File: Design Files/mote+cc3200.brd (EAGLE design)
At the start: 100 x 80 mm, 13 parts, among them IC1 TPS6306X, U1 CC3200

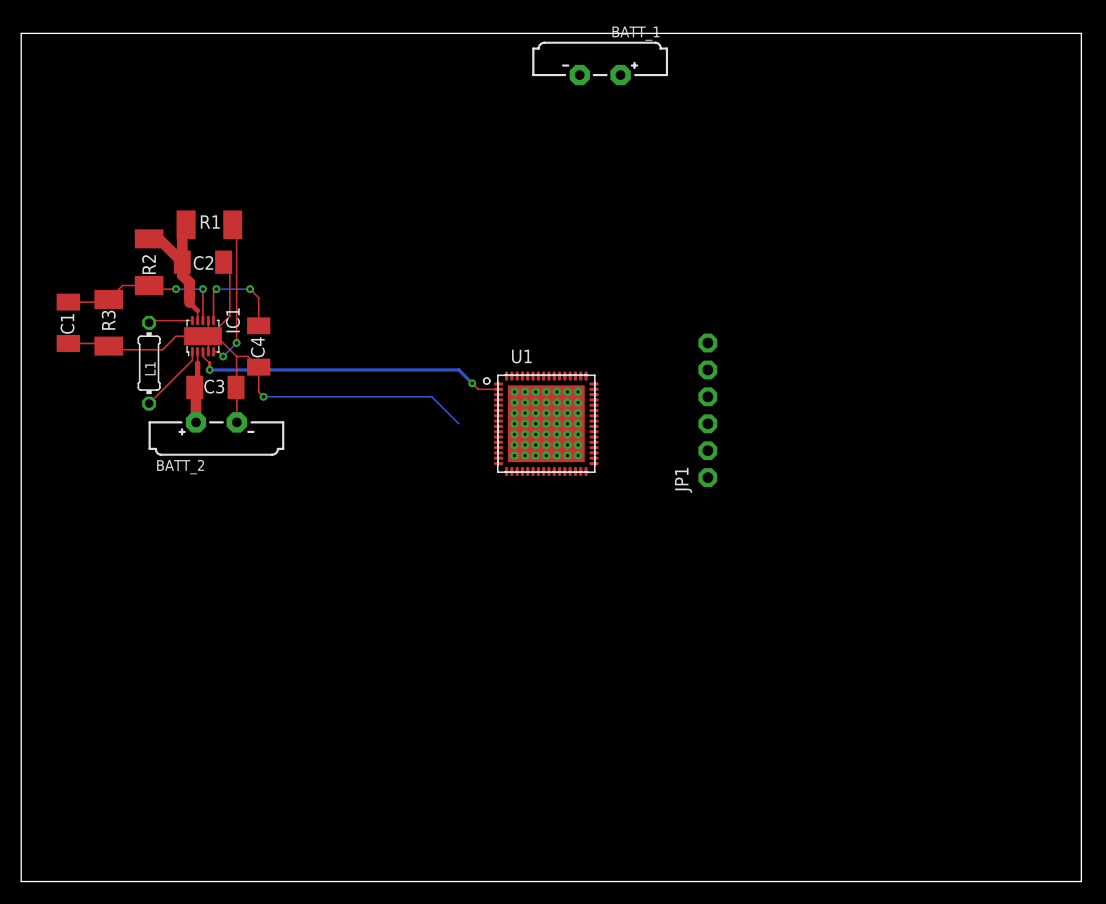
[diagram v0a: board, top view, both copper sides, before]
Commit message: Updated Design Files and Libraries
Some libraries included in the design were added.
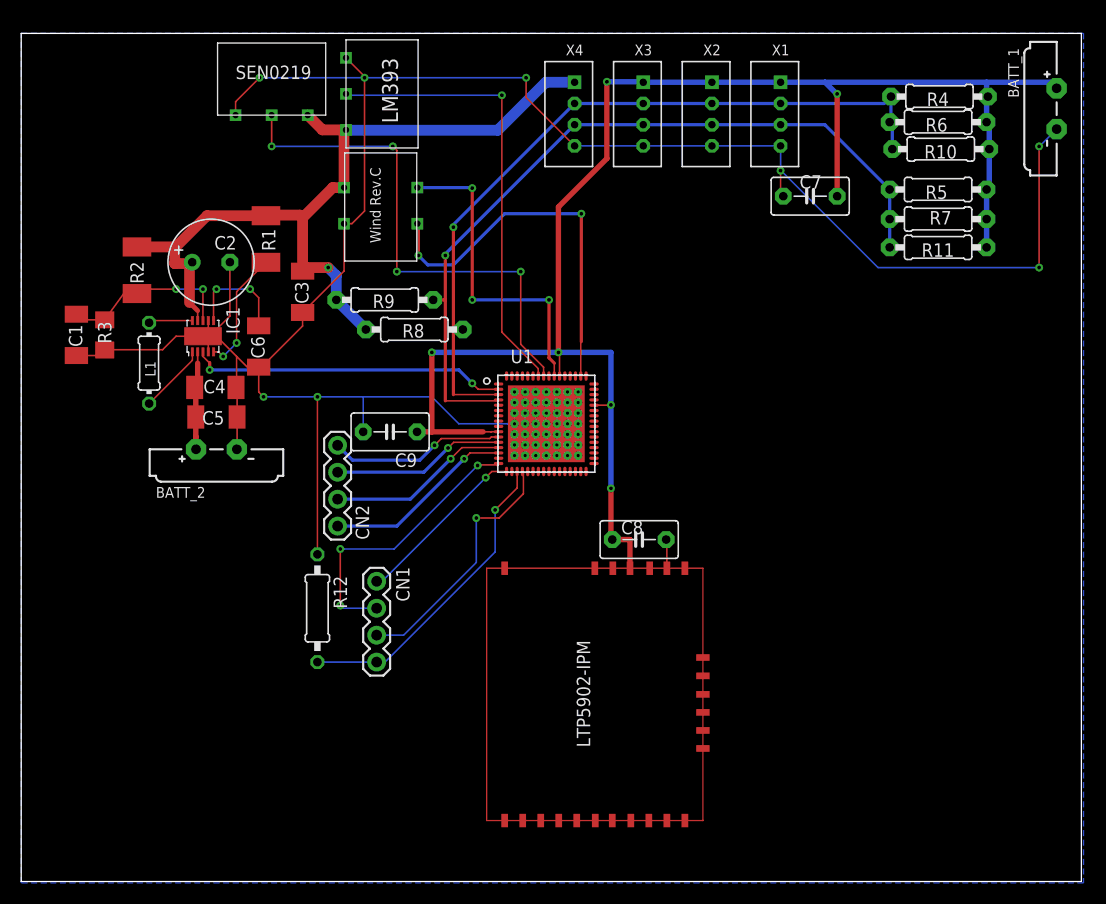
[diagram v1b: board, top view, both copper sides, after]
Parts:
- removed JP1: (no value), adafruit:1X06-CLEANBIG
- added C5: 10 uF, eagle-ltspice:C1808
- added C6: 0.1 uF, rcl:C1808
- added C7: 0.22 uF, capacitor-wima:C5B3.5
- added C8, C9: 0.1uF, capacitor-wima:C5B3.5
- added CN1: JTAG, adafruit:1X04-BIG
- added CN2: FLASH, adafruit:1X04-BIG
- added R10, R11, R4, R5, R6, R7, R8, R9: 2.2K, adafruit:0207/9
- added R12: 100K, resistor:0207/10
- added U2: WIND, WINDc:WIND
- added U3: SEN0219, SEN0219c:SEN0219
- added U4: LM393, LM393c:LM393
- added U5: LTP5902, LTP5902c:LTP5901
- added X1: HIH8121-021-001, con-JST PH:B4B-PH-K-S
- added X2: OPT3001, con-JST PH:B4B-PH-K-S
- added X3: ADXL362, con-JST PH:B4B-PH-K-S
- added X4: SEN0322, con-JST PH:B4B-PH-K-S
- C2: value 66 uF -> 56 uF; device eagle-ltspice:C1808 -> rcl:E3,5-8
- C3: value 20 uF -> 10 uF
- C4: value 0.1 uF -> 10 uF
- R1, R2: device eagle-ltspice:R2010 -> rcl:R5025
- R3: device eagle-ltspice:R2010 -> rcl:R1206
- moved BATT_1 41.9 mm to (96.3, 72.9), turned to 270 degrees
- moved C3 12.2 mm to (26.5, 55.6), turned to 270 degrees
- moved C4 5.62 mm to (18.3, 46.6), turned to 0 degrees
- moved R1 5.50 mm to (23.1, 60.6), turned to 90 degrees
- moved BATT_2 2.54 mm to (18.4, 39.4)
- moved C1 1.37 mm to (5.21, 51.6)
- moved R2 1.37 mm to (10.9, 57.7)
- moved R3 1.20 mm to (7.87, 51.6)
- moved C2 0.76 mm to (17.9, 58.4)
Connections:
- new net 3.3V: U5.P$1, U5.P$10, U5.P$11, U5.P$9
- new net AO_0S: U1.50, U2.P$4
- new net AO_1S: U1.55, U2.P$3
- new net AO_2S: U1.57, U3.P$2
- new net AO_3S: U1.58, U4.P$2
- new net DO_0: U5.P$2
- new net DO_1: U5.P$3
- new net FLASH_P_ENN: U5.P$21
- new net FLS_SPI_CLK: CN2.1, U1.11
- new net FLS_SPI_CS: CN2.4, U1.14
- new net FLS_SPI_DIN: CN2.3, U1.13
- new net FLS_SPI_DOUT: CN2.2, U1.12
- new net IPCS_MISO: U5.P$14
- new net IPCS_MOSI: U5.P$16
- new net IPCS_SCK: U5.P$17
- new net IPCS_SSN: U5.P$19
- new net N$1: CN1.4, R12.2, U1.19
- new net N$2: CN1.3, U1.20
- new net N$3: CN1.2, U1.16
- new net N$4: CN1.1, U1.17
- net +3.3V: now also C7.1, C8.2, C9.1, R10.1, R11.1, R4.1, R5.1, R6.1, R7.1, U5.P$22, X1.1, X2.1, X3.1
- net +3.6V: now also C4.1, C5.1; no longer C3.1
- net +5V: now also C2.+, C3.1, R8.1, R9.1, U2.P$1, U3.P$1, U4.P$1, X4.1; no longer C2.1
- net GND: now also C2.-, C5.2, C6.2, C7.2, C8.1, C9.2, R12.1, U2.P$2, U3.P$3, U4.P$3, U5.P$15, U5.P$18, U5.P$20, U5.P$23, U5.P$24, X1.4, X2.4, X3.4, X4.4; no longer C2.2
- net SCL: now also R10.2, R4.2, R6.2, R8.2, X1.2, X2.2, X3.2, X4.2
- net SDA: now also R11.2, R5.2, R7.2, R9.2, X1.3, X2.3, X3.3, X4.3
- net VAUX_TPS: now also C6.1; no longer C4.1
- net WK_UP: now also U5.P$4
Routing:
- net GND: track 60.9 -> 252.4 mm, vias 1 -> 8
- net +3.3V: track 0.00 -> 154.7 mm, vias 0 -> 6
- net SDA: track 0.00 -> 75.0 mm, vias 0 -> 1
- net SCL: track 0.00 -> 72.6 mm, vias 0 -> 1
- net +5V: track 13.8 -> 79.2 mm, vias 0 -> 1
- net AO_2S: track 0.00 -> 48.8 mm, vias 0 -> 4
- net AO_3S: track 0.00 -> 42.7 mm, vias 0 -> 1
- net AO_0S: track 0.00 -> 36.1 mm, vias 0 -> 2
- net AO_1S: track 0.00 -> 30.4 mm, vias 0 -> 3
- net N$1: track 0.00 -> 29.5 mm, vias 0 -> 1
- net N$3: track 0.00 -> 27.2 mm, vias 0 -> 3
- net N$2: track 0.00 -> 24.0 mm, vias 0 -> 1
- net FLS_SPI_CS: track 0.00 -> 18.0 mm, vias 0 -> 1
- net FLS_SPI_DIN: track 0.00 -> 17.2 mm, vias 0 -> 1
- net FLS_SPI_CLK: track 0.00 -> 16.7 mm, vias 0 -> 1
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- added copper zone on layer 16, net GND

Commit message: Updated design files.
Overwritten original mote+cc3200 files to revision 1.5. Added CAM data files in zip folder for PCB fabrication.
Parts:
- removed CN2: FLASH, adafruit:1X04-BIG
- removed R11: 2.2K, adafruit:0207/9
- removed R12: 100K, resistor:0207/10
- removed R2: 1 M, rcl:R5025
- removed U1: CC3200, CC3200:RGC0064A
- removed X4: SEN0322, con-JST PH:B4B-PH-K-S
- added AC1: ADXL345, ADXL345:CC-14-1
- added C10, C11: 10 pF, eagle-ltspice:C1808
- added C12, C16, C17, C19, C20, C22: 0.1 uF, rcl:C1808
- added C13: 0.1uF, capacitor-wima:C5B3.5
- added C14: 2.2 uF, eagle-ltspice:C1808
- added C15: 0.22 uF, capacitor-wima:C5B3.5
- added C18, C21: 10 uF, eagle-ltspice:C1808
- added D1: SP1002-01JTG, SamacSys_Parts:SOT132P220X110-3N
- added HDR1: 87831-1020, SamacSys_Parts:SHDR10W55P200_2X5_1265X630X640
- added IC2: W25Q80DLSNIG_TR, SamacSys_Parts:SOIC127P600X175-8N
- added JP1, JP2, JP3: (no value), eagle-ltspice:R0201
- added L2, L3: 2.2 uH, rcl:L3216C
- added LED1: 156120RS75000, SamacSys_Parts:LEDM3216X130N
- added PB1: FSMSM, SamacSys_Parts:FSMSM
- added Q1, Q2, Q3, Q4: FQU20N06LTU, SamacSys_Parts:TO229P250X658X985-3P
- added Q5: DMN2004WK-7, SamacSys_Parts:SC70-3_DCK
- added S1: EG1224, SamacSys_Parts:EG1224
- added U6: LM393, LM393c:LM393
- added Y1: 32.768 KHz, crystal-geyer_V1_0:7.0X5.0
- BATT_2: value BATTERY_BR1225/FA -> 12BH23P-GR; device 52101-101-REV-A_v16:BATTERY_BR1225/FA -> SamacSys_Parts:12BH23PGR
- C1: value 10 pF -> 10 uF
- C2: value 56 uF -> 10 uF; device rcl:E3,5-8 -> eagle-ltspice:C1808
- C3: value 10 uF -> 0.1uF; device eagle-ltspice:C1808 -> capacitor-wima:C5B3.5
- C4, C5: value 10 uF -> 0.1 uF; device eagle-ltspice:C1808 -> rcl:C1808
- C7: value 0.22 uF -> 10 pF; device capacitor-wima:C5B3.5 -> eagle-ltspice:C1808
- C8: value 0.1uF -> 56 uF; device capacitor-wima:C5B3.5 -> rcl:E3,5-8
- C9: value 0.1uF -> 10 uF; device capacitor-wima:C5B3.5 -> eagle-ltspice:C1808
- R1: value 1 M -> 100K; device rcl:R5025 -> resistor:0207/10
- R10: value 2.2K -> 270; device adafruit:0207/9 -> Resistor_Capacitor:RES_1206
- R3: value 111 K -> 1 M; device rcl:R1206 -> rcl:R5025
- R4: value 2.2K -> 111 K; device adafruit:0207/9 -> rcl:R1206
- R5: value 2.2K -> 1 M; device adafruit:0207/9 -> rcl:R5025
- R6, R7, R8: value 2.2K -> 100 K; device adafruit:0207/9 -> rcl:R1206
- R9: value 2.2K -> 10 K; device adafruit:0207/9 -> Resistor_Capacitor:RES_1206
- U2: value WIND -> Value; device WINDc:WIND -> CC3200:RGC0064A
- U3: value SEN0219 -> LTP5902; device SEN0219c:SEN0219 -> LTP5902c:LTP5902-MMCX
- U4: value LM393 -> WIND; device LM393c:LM393 -> WINDc:WIND
- U5: value LTP5902 -> SEN0219; device LTP5902c:LTP5901 -> SEN0219c:SEN0219
- X3: value ADXL362 -> SEN0322
- moved R4 87.6 mm to (5.33, 41.4), turned to 90 degrees
- moved R5 82.4 mm to (6.22, 46.6), turned to 0 degrees
- moved U3 80.2 mm to (83.6, 22.4), turned to 0 degrees
- moved C7 75.6 mm to (2.54, 41.3), turned to 270 degrees
- moved R6 73.0 mm to (31.2, 23.9), turned to 0 degrees
- moved R7 70.5 mm to (26.8, 25.0), turned to 270 degrees
- moved U5 65.6 mm to (23.6, 75.7), turned to 270 degrees
- moved C8 46.0 mm to (13.8, 43.9), turned to 0 degrees
- moved C4 36.7 mm to (54.5, 53.0), turned to 90 degrees
- moved C5 35.8 mm to (48.1, 23.9)
- moved R9 35.7 mm to (54.7, 25.7)
- moved R1 31.5 mm to (23.6, 29.1), turned to 270 degrees
- moved BATT_2 29.1 mm to (29.4, 12.4), turned to 180 degrees
- moved C2 27.8 mm to (14.5, 30.9)
- moved U2 25.7 mm to (49.5, 43.2)
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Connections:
- removed net 3.3V: U5.P$1, U5.P$10, U5.P$11, U5.P$9
- removed net AO_0S: U1.50, U2.P$4
- removed net AO_1S: U1.55, U2.P$3
- removed net AO_2S: U1.57, U3.P$2
- removed net AO_3S: U1.58, U4.P$2
- removed net DCDC_ANA_SW: U1.38
- removed net DCDC_DIG_SW: U1.43
- removed net DO_0: U5.P$2
- removed net DO_1: U5.P$3
- removed net LDO_IN1: U1.36
- removed net LDO_IN2: U1.25
- removed net N$1: CN1.4, R12.2, U1.19
- removed net N$2: CN1.3, U1.20
- removed net N$3: CN1.2, U1.16
- removed net N$4: CN1.1, U1.17
- removed net VDD_DIG1: U1.9
- removed net VDD_DIG2: U1.56
- removed net VDD_PLL: U1.24
- removed net WK_UP: IC1.3, U1.2, U5.P$4
- new net DC_ANA2: JP2.1, U2.46
- new net DC_DIGSW: L3.2, U2.43
- new net GPIO12: Q4.1, U2.3
- new net GPIO13: Q1.1, U2.4
- new net GPIO14: Q2.1, U2.5
- new net GPIO15: Q3.1, U2.6
- new net GPIO2: U2.57, U4.P$4
- new net GPIO22: IC1.3, U2.15
- new net GPIO3: U2.58, U4.P$3
- new net GPIO31: JP2.2
- new net GPIO4: U2.59, U5.P$2
- new net GPIO5: U2.60, U6.P$2
- new net JTCK: JP1.2, U2.21
- new net L2_ANA: L2.2, U2.38
- new net LED1: LED1.2, R10.2
- new net Q1+: AC1.2, AC1.4, AC1.5, C15.2, Q1.2, U6.P$3, X1.4, X2.4
- new net Q2+: Q2.2, U4.P$2
- new net Q3+: Q3.2, U5.P$3
- new net Q4+: Q4.2, X3.4
- new net RESETN: HDR1.6, Q5.3, U3.P15
- new net RST_BTN: C13.2, PB1.1, Q5.1, R9.2
- new net TCK: CN1.4, JP1.1, R1.2, U2.19
- new net TDI: CN1.2, U2.16
- new net TDO: CN1.1, U2.17
- new net TMS: CN1.3, U2.20
- new net UARTC0_RX: HDR1.10, U2.8, U3.P32
- new net UARTC0_TX: HDR1.9, U2.7, U3.P31
- new net VCC_DCDC: JP3.2
- new net VDD_DIG: C16.1, C17.1, C18.1, L3.1, U2.56, U2.9
- new net VDD_PULL: C5.1, U2.24
- new net VIN_DCDC_PA: U2.39
- new net VSUPPLY: HDR1.7
- new net XTAL1: C11.1, U2.51, Y1.3
- new net XTAL2: C10.1, U2.52, Y1.1
- net +3.3V: now also AC1.1, C12.1, C14.1, C15.1, C3.1, D1.1, IC2.3, IC2.7, IC2.8, PB1.2, R8.2, S1.1, U2.10, U2.37, U2.44, U2.54, U3.P55, U6.P$1; no longer C7.1, C8.2, C9.1, R11.1, R4.1, R5.1, R6.1, R7.1, U1.10, U1.37, U1.39, U1.44, U1.54, U5.P$22, X3.1
- net +3.6V: now also BATT_2.2, C1.1, C2.1; no longer BATT_2.+, C4.1, C5.1
- net +5V: now also C8.+, C9.1, R3.2, R5.2, U5.P$1, X3.1; no longer C2.+, C3.1, R1.2, R2.2, R8.1, R9.1, U2.P$1, U3.P$1, X4.1
- net DCDC_PA_OUT: now also U2.42; no longer U1.42
- net DCDC_PA_SW_N: now also U2.41; no longer U1.41
- net DCDC_PA_SW_P: now also U2.40; no longer U1.40
- net FB_TPS: now also C7.1, R4.2, R5.1; no longer C1.1, R2.1, R3.2
- net FLASH_P_ENN: now also HDR1.2, U3.P51; no longer U5.P$21
- net FLS_SPI_CLK: now also IC2.6, R6.1, U2.11; no longer CN2.1, U1.11
- net FLS_SPI_CS: now also IC2.1, R8.1, U2.14; no longer CN2.4, U1.14
- net FLS_SPI_DIN: now also IC2.2, U2.13; no longer CN2.3, U1.13
- net FLS_SPI_DOUT: now also IC2.5, R7.1, U2.12; no longer CN2.2, U1.12
- net GND: now also BATT_2.1, C10.2, C11.2, C12.2, C13.1, C14.2, C16.2, C17.2, C18.2, C19.2, C2.2, C20.2, C21.2, C22.2, C8.-, D1.2, HDR1.8, IC2.4, LED1.1, Q1.3, Q2.3, Q3.3, Q4.3, Q5.2, R1.1, R4.1, R6.2, R7.2, R9.1, S1.2, U2.65, U2.V, U2.V_1, U2.V_10, U2.V_11, U2.V_12, U2.V_13, U2.V_14, U2.V_15, U2.V_16, U2.V_17, U2.V_18, U2.V_19, U2.V_2, U2.V_20, U2.V_21, U2.V_22, U2.V_23, U2.V_24, U2.V_25, U2.V_26, U2.V_27, U2.V_28, U2.V_29, U2.V_3, U2.V_30, U2.V_31, U2.V_32, U2.V_33, U2.V_34, U2.V_35, U2.V_36, U2.V_37, U2.V_38, U2.V_39, U2.V_4, U2.V_40, U2.V_41, U2.V_42, U2.V_43, U2.V_44, U2.V_45, U2.V_46, U2.V_47, U2.V_48, U2.V_5, U2.V_6, U2.V_7, U2.V_8, U2.V_9, U3.P1, U3.P11, U3.P20, U3.P30, U3.P34, U3.P37, U3.P42, U3.P49, U3.P56, U3.P66; no longer BATT_2.-, C2.-, C8.1, R12.1, R3.1, U1.65, U2.P$2, U3.P$3, U4.P$3, U5.P$15, U5.P$18, U5.P$20, U5.P$23, U5.P$24, X1.4, X2.4, X3.4, X4.4
- net IPCS_MISO: now also HDR1.5, U3.P33; no longer U5.P$14
- net IPCS_MOSI: now also U3.P35; no longer U5.P$16
- net IPCS_SCK: now also HDR1.3; no longer U5.P$17
- net IPCS_SSN: now also HDR1.1, U3.P39; no longer U5.P$19
- net PG_TPS: now also R3.1; no longer R1.1
- net SCL: now also AC1.14, U2.1; no longer R10.2, R4.2, R6.2, R8.2, U1.3, X4.2
- net SDA: now also AC1.13, U2.2; no longer R11.2, R5.2, R7.2, R9.2, U1.4, X4.3
- net VDD_ANA1: now also C19.1, C20.1, C21.1, C22.1, L2.1, U2.25, U2.36, U2.48; no longer U1.48
- net VDD_ANA2: now also JP3.1, U2.47; no longer U1.47
- net VDD_PA_IN: now also U2.33; no longer U1.33
- net VDD_RAM: now also C4.1, U2.49; no longer U1.49
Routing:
- net GND: track 252.4 -> 407.6 mm, vias 8 -> 14
- net +3.3V: track 154.7 -> 272.4 mm, vias 6 -> 10
- net UARTC0_RX: track 0.00 -> 110.2 mm, vias 0 -> 2
- net UARTC0_TX: track 0.00 -> 101.0 mm, vias 0 -> 5
- net VDD_DIG: track 0.00 -> 89.9 mm, vias 0 -> 3
- net GPIO5: track 0.00 -> 66.8 mm, vias 0 -> 2
- net Q1+: track 0.00 -> 61.1 mm, vias 0 -> 2
- net VDD_ANA1: track 0.00 -> 51.0 mm, vias 0 -> 4
- net GPIO15: track 0.00 -> 49.0 mm, vias 0 -> 1
- net AO_2S: track 48.8 -> 0.00 mm, vias 4 -> 0
- net GPIO4: track 0.00 -> 47.7 mm, vias 0 -> 4
- net IPCS_SSN: track 0.00 -> 47.2 mm, vias 0 -> 1
- net RST_BTN: track 0.00 -> 45.9 mm, vias 0 -> 2
- net AO_3S: track 42.7 -> 0.00 mm, vias 1 -> 0
- net Q2+: track 0.00 -> 42.1 mm, vias 0 -> 3
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- added copper zone on layer 1, net GND

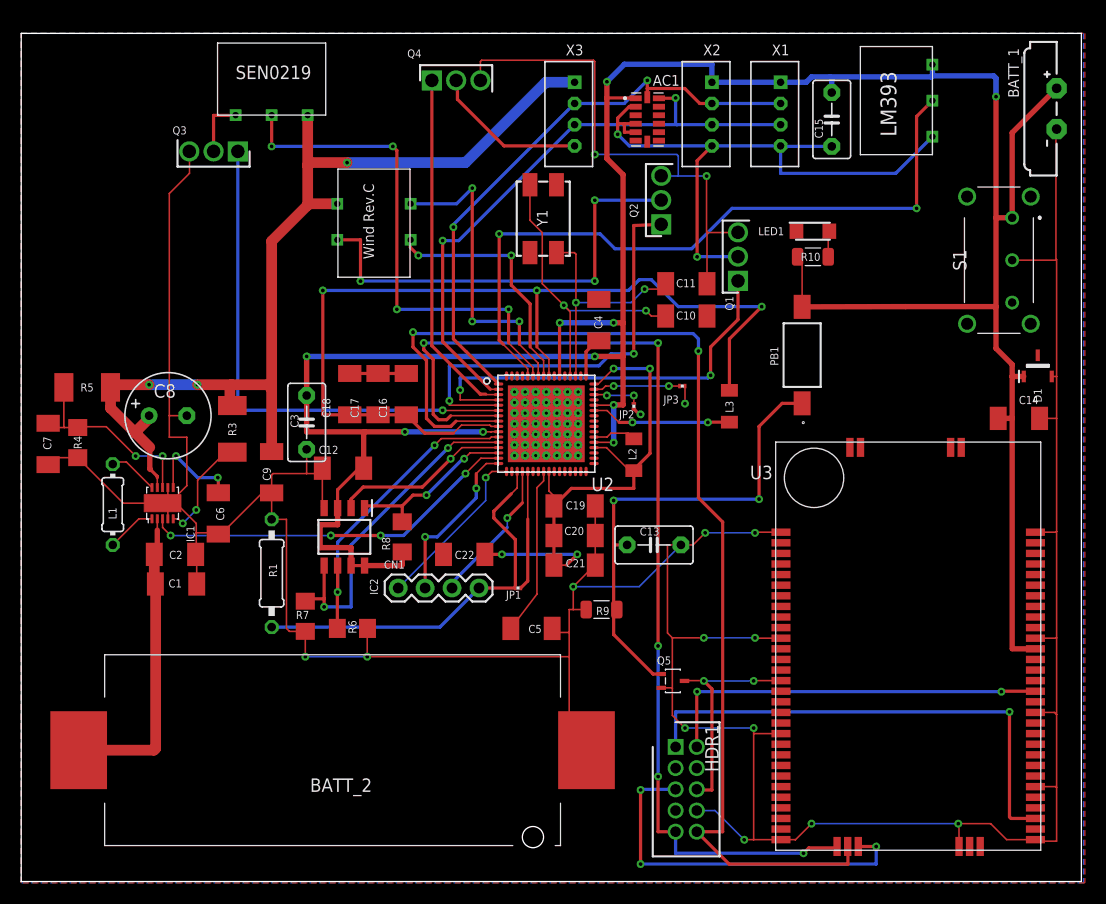
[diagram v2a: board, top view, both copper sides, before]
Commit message: Design files revised.
Added SOP connections to the design.
Ground stitched vias on the board were placed.
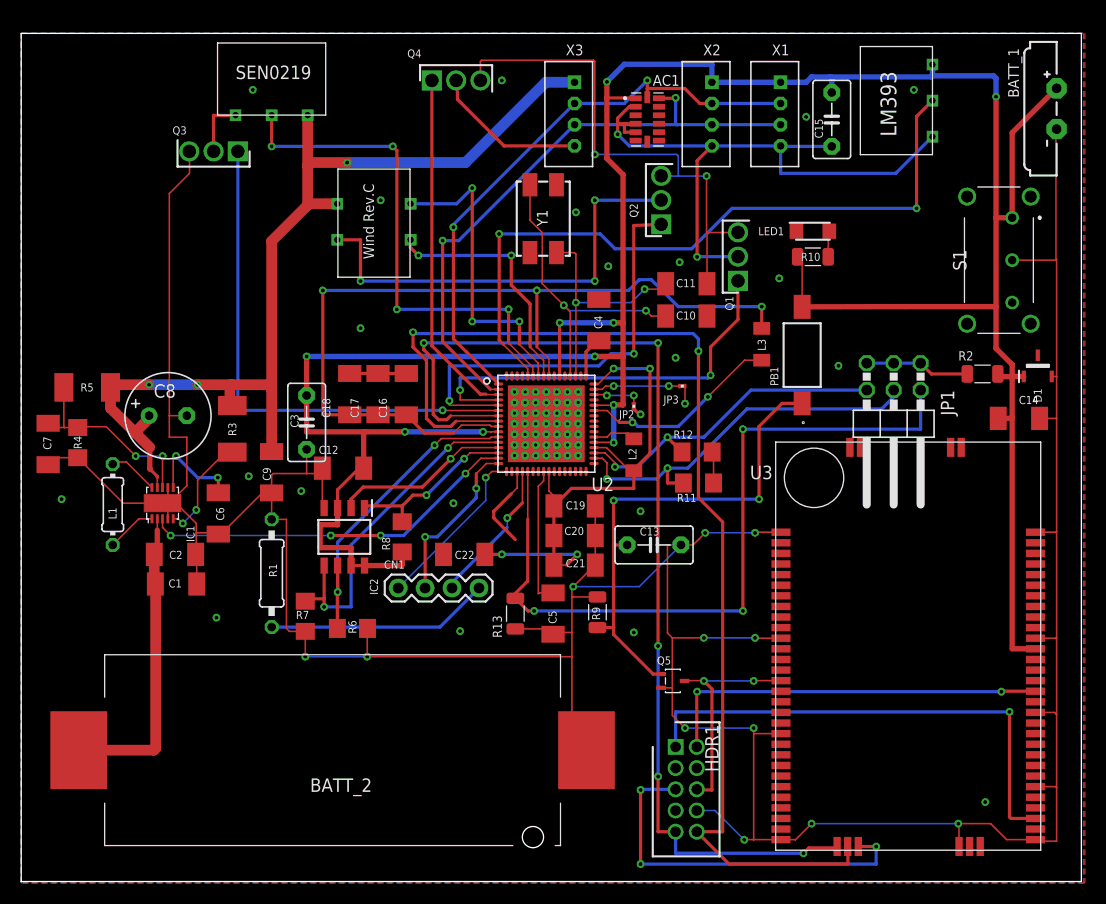
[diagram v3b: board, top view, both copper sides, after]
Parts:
- added R11, R12: 100 K, rcl:R1206
- added R13: 2.7k, Resistor_Capacitor:RES_1206
- added R2: 270, Resistor_Capacitor:RES_1206
- JP1: device eagle-ltspice:R0201 -> pinhead:2X03/90
- moved JP1 38.4 mm to (82.3, 42.5), turned to 180 degrees
- moved L3 6.59 mm to (69.8, 50.7)
- moved C5 2.47 mm to (50.2, 25.3), turned to 270 degrees
- moved R9 0.46 mm to (54.4, 25.4), turned to 270 degrees
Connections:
- removed net JTCK: JP1.2, U2.21
- new net JP1_PWR: JP1.1, JP1.3, JP1.5, R2.1
- new net SOP0: JP1.6, R12.1, U2.35
- new net SOP1: JP1.4, R11.1, U2.34
- new net SOP2: JP1.2, R13.2, U2.21
- net +3.3V: now also R2.2
- net GND: now also R11.2, R12.2, R13.1
- net TCK: no longer JP1.1
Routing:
- net SOP2: track 0.00 -> 72.0 mm, vias 0 -> 3
- net SOP1: track 0.00 -> 36.7 mm, vias 0 -> 2
- net SOP0: track 0.00 -> 31.5 mm, vias 0 -> 2
- net JTCK: track 11.3 -> 0.00 mm
- net JP1_PWR: track 0.00 -> 9.90 mm
- net TCK: track 37.3 -> 29.3 mm
- net GND: track 407.6 -> 415.4 mm, vias 14 -> 35
- net VDD_DIG: track 89.9 -> 82.8 mm
- net DC_DIGSW: track 13.2 -> 19.0 mm
- net VDD_PULL: track 15.9 -> 13.1 mm
- net +3.3V: track 272.4 -> 274.3 mm
- net RST_BTN: track 45.9 -> 47.0 mm
